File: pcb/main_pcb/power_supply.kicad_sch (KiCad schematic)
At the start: 36 parts, among them J12 Screw_Terminal_01x02, J13 Conn_01x02_Male, Q1 Q_PMOS_GDS, SW1 SW_SPDT, U1 LM3151/2/3, U5 TPIC74101

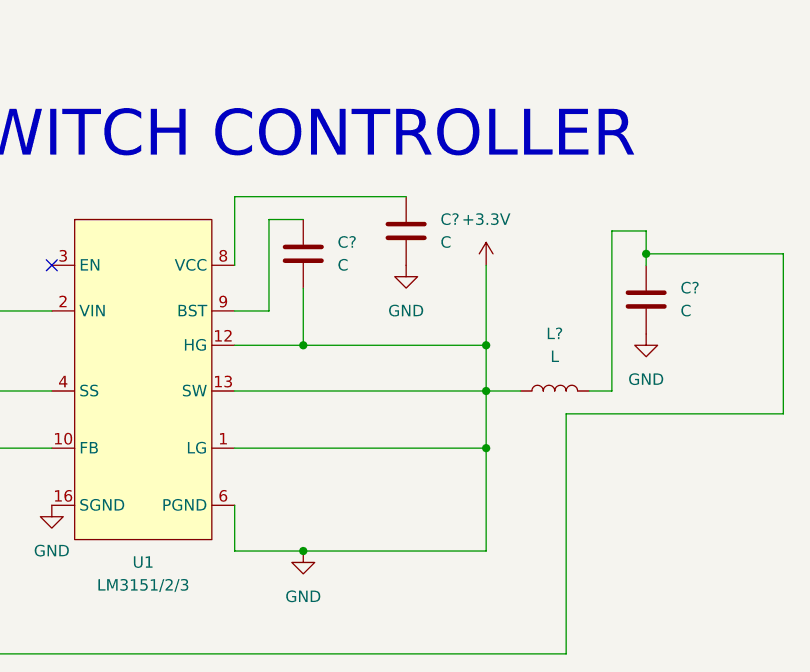
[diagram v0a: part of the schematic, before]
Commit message: ADDED MOSFETS
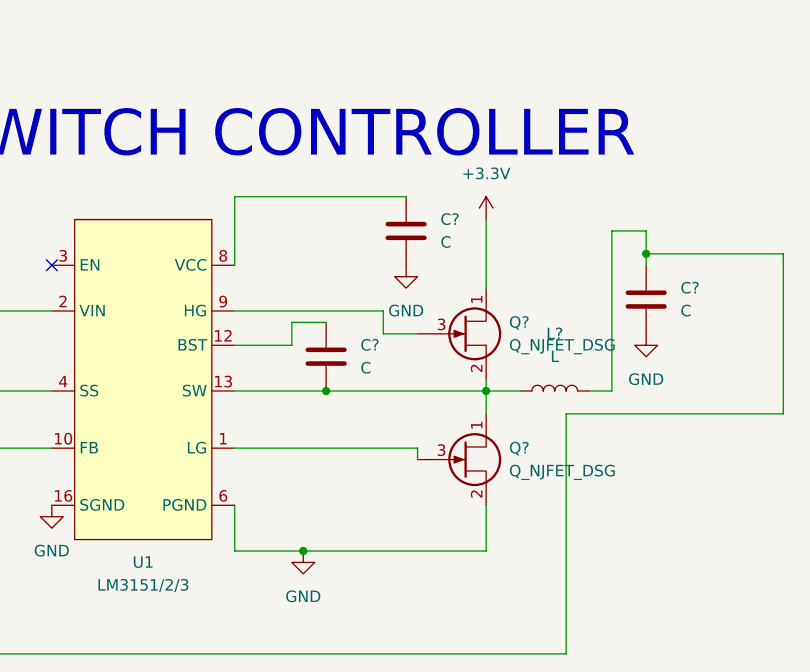
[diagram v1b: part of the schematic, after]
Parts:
- added Q? (x2): Q_NJFET_DSG, symbol Device:Q_NJFET_DSG
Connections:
- net +3.3V: now also Q?.1 (D); no longer C1.2, C10.2, C11.2, C13.2, C14.2, C15.2, C2.2, C3.2, C6.2, C7.2, C?.2, C?.2, C?.2, C?.2, C?.2, D4.2 (A), J12.1 (Pin_1), L?.2, Q1.1 (G), R10.1, R13.2, R7.1, R9.2, U1.1 (LG), U1.12 (HG), U1.13 (SW), U1.16 (SGND), U1.6 (PGND), U5.1 (SCR1), U5.11 (CLP), U5.16 (GND), U5.20 (SCR0), U5.21 (PAD), U5.6 (PGND)
- net at U1.9 (HG): now also Q?.3 (G); no longer C?.1
- new net: C?.2, L?.2, Q?.1 (D), Q?.2 (S), U1.13 (SW)
- new net: Q?.3 (G), U1.1 (LG)
- new net: C?.1, U1.12 (BST)
- new net GND: C1.2, C10.2, C11.2, C13.2, C14.2, C15.2, C2.2, C3.2, C6.2, C7.2, C?.2, C?.2, C?.2, C?.2, D4.2 (A), J12.1 (Pin_1), Q1.1 (G), Q?.2 (S), R10.1, R13.2, R7.1, R9.2, U1.16 (SGND), U1.6 (PGND), U5.1 (SCR1), U5.11 (CLP), U5.16 (GND), U5.20 (SCR0), U5.21 (PAD), U5.6 (PGND)
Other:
- moved on the sheet: C?
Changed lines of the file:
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@@
   (junction (at 139.7 43.815) (diameter 0) (color 0 0 0 0)
   )
-  (junction (at 142.24 156.21) (diameter 0) (color 0 0 0 0)
-  )
   (junction (at 142.24 179.07) (diameter 0) (color 0 0 0 0)
   )
@@
   (junction (at 213.36 71.12) (diameter 0) (color 0 0 0 0)
   )
+  (junction (at 144.78 161.29) (diameter 0) (color 0 0 0 0)
+  )
   (junction (at 137.16 87.63) (diameter 0) (color 0 0 0 0)
   )
@@
   )
   (junction (at 197.485 90.17) (diameter 0) (color 0 0 0 0)
-  )
-  (junction (at 162.56 156.21) (diameter 0) (color 0 0 0 0)
-  )
-  (junction (at 162.56 167.64) (diameter 0) (color 0 0 0 0)
   )
   (junction (at 225.425 51.435) (diameter 0) (color 0 0 0 0)
@@
     (stroke (width 0) (type default) (color 0 0 0 0))
   )
+  (wire (pts (xy 162.56 142.24) (xy 162.56 149.86))
+    (stroke (width 0) (type default) (color 0 0 0 0))
+  )
   (wire (pts (xy 70.485 50.165) (xy 70.485 43.815))
     (stroke (width 0) (type default) (color 0 0 0 0))
@@
     (stroke (width 0) (type default) (color 0 0 0 0))
   )
+  (wire (pts (xy 162.56 161.29) (xy 162.56 163.83))
+    (stroke (width 0) (type default) (color 0 0 0 0))
+  )
   (wire (pts (xy 161.925 91.44) (xy 161.925 98.425))
     (stroke (width 0) (type default) (color 0 0 0 0))
@@
     (stroke (width 0) (type default) (color 0 0 0 0))
   )
+  (wire (pts (xy 140.97 156.21) (xy 140.97 153.67))
+    (stroke (width 0) (type default) (color 0 0 0 0))
+  )
   (wire (pts (xy 179.07 46.355) (xy 180.975 46.355))
     (stroke (width 0) (type default) (color 0 0 0 0))
   )
+  (wire (pts (xy 134.62 167.64) (xy 154.94 167.64))
+    (stroke (width 0) (type default) (color 0 0 0 0))
+  )
   (wire (pts (xy 195.58 146.05) (xy 180.34 146.05))
     (stroke (width 0) (type default) (color 0 0 0 0))
@@
     (stroke (width 0) (type default) (color 0 0 0 0))
   )
-  (wire (pts (xy 142.24 149.86) (xy 142.24 156.21))
-    (stroke (width 0) (type default) (color 0 0 0 0))
-  )
   (wire (pts (xy 123.19 88.9) (xy 123.19 87.63))
     (stroke (width 0) (type default) (color 0 0 0 0))
@@
     (stroke (width 0) (type default) (color 0 0 0 0))
   )
-  (wire (pts (xy 162.56 147.32) (xy 162.56 156.21))
-    (stroke (width 0) (type default) (color 0 0 0 0))
-  )
   (wire (pts (xy 110.49 69.85) (xy 110.49 71.755))
     (stroke (width 0) (type default) (color 0 0 0 0))
@@
   )
   (wire (pts (xy 213.36 71.12) (xy 213.36 72.39))
+    (stroke (width 0) (type default) (color 0 0 0 0))
+  )
+  (wire (pts (xy 144.78 161.29) (xy 162.56 161.29))
     (stroke (width 0) (type default) (color 0 0 0 0))
   )
@@
     (stroke (width 0) (type default) (color 0 0 0 0))
   )
-  (wire (pts (xy 162.56 156.21) (xy 162.56 161.29))
+  (wire (pts (xy 151.13 154.94) (xy 154.94 154.94))
     (stroke (width 0) (type default) (color 0 0 0 0))
   )
@@
     (stroke (width 0) (type default) (color 0 0 0 0))
   )
-  (wire (pts (xy 162.56 167.64) (xy 162.56 179.07))
+  (wire (pts (xy 162.56 160.02) (xy 162.56 161.29))
+    (stroke (width 0) (type default) (color 0 0 0 0))
+  )
+  (wire (pts (xy 151.13 152.4) (xy 151.13 154.94))
     (stroke (width 0) (type default) (color 0 0 0 0))
   )
@@
   )
   (wire (pts (xy 123.19 80.01) (xy 172.085 80.01))
+    (stroke (width 0) (type default) (color 0 0 0 0))
+  )
+  (wire (pts (xy 162.56 173.99) (xy 162.56 179.07))
     (stroke (width 0) (type default) (color 0 0 0 0))
   )
@@
     (stroke (width 0) (type default) (color 0 0 0 0))
   )
-  (wire (pts (xy 134.62 156.21) (xy 142.24 156.21))
-    (stroke (width 0) (type default) (color 0 0 0 0))
-  )
   (wire (pts (xy 207.01 76.835) (xy 207.01 78.74))
     (stroke (width 0) (type default) (color 0 0 0 0))
@@
     (stroke (width 0) (type default) (color 0 0 0 0))
   )
-  (wire (pts (xy 134.62 161.29) (xy 162.56 161.29))
+  (wire (pts (xy 134.62 161.29) (xy 144.78 161.29))
     (stroke (width 0) (type default) (color 0 0 0 0))
   )
@@
     (stroke (width 0) (type default) (color 0 0 0 0))
   )
-  (wire (pts (xy 138.43 152.4) (xy 138.43 142.24))
-    (stroke (width 0) (type default) (color 0 0 0 0))
-  )
   (wire (pts (xy 190.5 48.895) (xy 190.5 46.355))
     (stroke (width 0) (type default) (color 0 0 0 0))
@@
     (stroke (width 0) (type default) (color 0 0 0 0))
   )
+  (wire (pts (xy 154.94 167.64) (xy 154.94 168.91))
+    (stroke (width 0) (type default) (color 0 0 0 0))
+  )
   (wire (pts (xy 154.305 96.52) (xy 154.305 98.425))
     (stroke (width 0) (type default) (color 0 0 0 0))
@@
     (stroke (width 0) (type default) (color 0 0 0 0))
   )
-  (wire (pts (xy 134.62 167.64) (xy 162.56 167.64))
-    (stroke (width 0) (type default) (color 0 0 0 0))
-  )
   (wire (pts (xy 67.31 57.785) (xy 67.31 59.69))
     (stroke (width 0) (type default) (color 0 0 0 0))
   )
-  (wire (pts (xy 134.62 152.4) (xy 138.43 152.4))
+  (wire (pts (xy 134.62 152.4) (xy 151.13 152.4))
     (stroke (width 0) (type default) (color 0 0 0 0))
   )
@@
     (stroke (width 0) (type default) (color 0 0 0 0))
   )
+  (wire (pts (xy 134.62 156.21) (xy 140.97 156.21))
+    (stroke (width 0) (type default) (color 0 0 0 0))
+  )
   (wire (pts (xy 197.485 43.815) (xy 197.485 40.005))
     (stroke (width 0) (type default) (color 0 0 0 0))
@@
     (stroke (width 0) (type default) (color 0 0 0 0))
   )
-  (wire (pts (xy 142.24 156.21) (xy 162.56 156.21))
-    (stroke (width 0) (type default) (color 0 0 0 0))
-  )
   (wire (pts (xy 238.125 81.28) (xy 225.425 81.28))
     (stroke (width 0) (type default) (color 0 0 0 0))
   )
-  (wire (pts (xy 138.43 142.24) (xy 142.24 142.24))
+  (wire (pts (xy 140.97 153.67) (xy 144.78 153.67))
     (stroke (width 0) (type default) (color 0 0 0 0))
   )
@@
   )
   (wire (pts (xy 190.5 43.815) (xy 190.5 46.355))
-    (stroke (width 0) (type default) (color 0 0 0 0))
-  )
-  (wire (pts (xy 162.56 161.29) (xy 162.56 167.64))
     (stroke (width 0) (type default) (color 0 0 0 0))
   )
@@
     )
     (property "Datasheet" "~" (id 3) (at 80.01 46.355 0)
+      (effects (font (size 1.27 1.27)) hide)
+    )
+    (pin "1")
+    (pin "2")
+    (pin "3")
+  )
+  (symbol (lib_id "Device:Q_NJFET_DSG") (at 160.02 154.94 0) (unit 1)
+    (in_bom yes) (on_board yes) (fields_autoplaced)
+    (property "Reference" "Q?" (id 0) (at 165.1 153.6699 0)
+      (effects (font (size 1.27 1.27)) (justify left))
+    )
+    (property "Value" "Q_NJFET_DSG" (id 1) (at 165.1 156.2099 0)
+      (effects (font (size 1.27 1.27)) (justify left))
+    )
+    (property "Footprint" "" (id 2) (at 165.1 152.4 0)
+      (effects (font (size 1.27 1.27)) hide)
+    )
+    (property "Datasheet" "~" (id 3) (at 160.02 154.94 0)
       (effects (font (size 1.27 1.27)) hide)
     )
@@
     (pin "1")
   )
+  (symbol (lib_id "Device:Q_NJFET_DSG") (at 160.02 168.91 0) (unit 1)
+    (in_bom yes) (on_board yes) (fields_autoplaced)
+    (property "Reference" "Q?" (id 0) (at 165.1 167.6399 0)
+      (effects (font (size 1.27 1.27)) (justify left))
+    )
+    (property "Value" "Q_NJFET_DSG" (id 1) (at 165.1 170.1799 0)
+      (effects (font (size 1.27 1.27)) (justify left))
+    )
+    (property "Footprint" "" (id 2) (at 165.1 166.37 0)
+      (effects (font (size 1.27 1.27)) hide)
+    )
+    (property "Datasheet" "~" (id 3) (at 160.02 168.91 0)
+      (effects (font (size 1.27 1.27)) hide)
+    )
+    (pin "1")
+    (pin "2")
+    (pin "3")
+  )
   (symbol (lib_id "Device:C") (at 123.19 57.15 0) (unit 1)
     (in_bom yes) (on_board yes) (fields_autoplaced)
@@
     (pin "1")
   )
-  (symbol (lib_id "power:+3.3V") (at 162.56 147.32 0) (unit 1)
-    (in_bom yes) (on_board yes) (fields_autoplaced)
-    (property "Reference" "#PWR?" (id 0) (at 162.56 151.13 0)
-      (effects (font (size 1.27 1.27)) hide)
-    )
-    (property "Value" "+3.3V" (id 1) (at 162.56 142.24 0))
-    (property "Footprint" "" (id 2) (at 162.56 147.32 0)
-      (effects (font (size 1.27 1.27)) hide)
-    )
-    (property "Datasheet" "" (id 3) (at 162.56 147.32 0)
-      (effects (font (size 1.27 1.27)) hide)
-    )
-    (pin "1")
-  )
-  (symbol (lib_id "Device:C") (at 142.24 146.05 0) (unit 1)
-    (in_bom yes) (on_board yes) (fields_autoplaced)
-    (property "Reference" "C?" (id 0) (at 146.05 144.7799 0)
-      (effects (font (size 1.27 1.27)) (justify left))
-    )
-    (property "Value" "C" (id 1) (at 146.05 147.3199 0)
-      (effects (font (size 1.27 1.27)) (justify left))
-    )
-    (property "Footprint" "" (id 2) (at 143.2052 149.86 0)
-      (effects (font (size 1.27 1.27)) hide)
-    )
-    (property "Datasheet" "~" (id 3) (at 142.24 146.05 0)
-      (effects (font (size 1.27 1.27)) hide)
-    )
+  (symbol (lib_id "power:+3.3V") (at 162.56 142.24 0) (unit 1)
+    (in_bom yes) (on_board yes) (fields_autoplaced)
+    (property "Reference" "#PWR?" (id 0) (at 162.56 146.05 0)
+      (effects (font (size 1.27 1.27)) hide)
+    )
+    (property "Value" "+3.3V" (id 1) (at 162.56 137.16 0))
+    (property "Footprint" "" (id 2) (at 162.56 142.24 0)
+      (effects (font (size 1.27 1.27)) hide)
+    )
+    (property "Datasheet" "" (id 3) (at 162.56 142.24 0)
+      (effects (font (size 1.27 1.27)) hide)
+    )
+    (pin "1")
+  )
+  (symbol (lib_id "Device:C") (at 144.78 157.48 0) (unit 1)
+    (in_bom yes) (on_board yes) (fields_autoplaced)
+    (property "Reference" "C?" (id 0) (at 148.59 156.2099 0)
+      (effects (font (size 1.27 1.27)) (justify left))
+    )
+    (property "Value" "C" (id 1) (at 148.59 158.7499 0)
+      (effects (font (size 1.27 1.27)) (justify left))
+    )
+    (property "Footprint" "" (id 2) (at 145.7452 161.29 0)
+      (effects (font (size 1.27 1.27)) hide)
+    )
+    (property "Datasheet" "~" (id 3) (at 144.78 157.48 0)
+      (effects (font (size 1.27 1.27)) hide)
+    )

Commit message: changes to pcb
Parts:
- removed C1: 330uF, Capacitor_SMD:CP_Elec_10x10.5, symbol Device:C_Polarized_US
- removed C10, C11, C2: 0.1uF, Capacitor_SMD:C_0603_1608Metric_Pad1.08x0.95mm_HandSolder, symbol Device:C
- removed C13: 100uF, Capacitor_SMD:CP_Elec_8x10.5, symbol Device:C_Polarized_US
- removed C14, C15: 22uF, Capacitor_SMD:CP_Elec_8x10.5, symbol Device:C_Polarized_US
- removed C3, C6: 470nF, Capacitor_SMD:C_0603_1608Metric_Pad1.08x0.95mm_HandSolder, symbol Device:C
- removed C7: 150nF, Capacitor_SMD:C_0603_1608Metric_Pad1.08x0.95mm_HandSolder, symbol Device:C
- removed C8, C9: 4.7nF, Capacitor_SMD:C_0603_1608Metric_Pad1.08x0.95mm_HandSolder, symbol Device:C
- removed D1, D2: LED, LED_THT:LED_D5.0mm, symbol Device:LED
- removed D4: D_Schottky, Diode_SMD:D_TUMD2, symbol Device:D_Schottky
- removed J12: Screw_Terminal_01x02, TerminalBlock:TerminalBlock_bornier-2_P5.08mm, symbol Connector:Screw_Terminal_01x02
- removed J13: Conn_01x02_Male, Connector_PinHeader_2.54mm:PinHeader_1x02_P2.54mm_Vertical, symbol Connector:Conn_01x02_Male
- removed L1, L2: 22uH, custom_footprints:L_SRR1050HA_Bourns, symbol Device:L
- removed Q1: Q_PMOS_GDS, Package_TO_SOT_SMD:TO-263-3_TabPin2, symbol Device:Q_PMOS_GDS
- removed R10: 0, Resistor_SMD:R_0603_1608Metric_Pad0.98x0.95mm_HandSolder, symbol Device:R
- removed R11, R12: 5k, Resistor_SMD:R_0603_1608Metric_Pad0.98x0.95mm_HandSolder, symbol Device:R
- removed R13: 470, Resistor_SMD:R_0603_1608Metric_Pad0.98x0.95mm_HandSolder, symbol Device:R
- removed R7: 12k, Resistor_SMD:R_0603_1608Metric_Pad0.98x0.95mm_HandSolder, symbol Device:R
- removed R8: 3.3k, Resistor_SMD:R_0603_1608Metric_Pad0.98x0.95mm_HandSolder, symbol Device:R
- removed R9: 4.53k, Resistor_SMD:R_0603_1608Metric_Pad0.98x0.95mm_HandSolder, symbol Device:R
- removed SW1: SW_SPDT, custom_footprints:SW_SPDT_NKK_MS12AANW03, symbol Switch:SW_SPDT
- removed U5: TPIC74101, custom_footprints:HTSSOP-20-1EP_4.4x6.5mm_P0.65mm_EP3.4x6.5mm_ThermalVias, symbol sym_library:TPIC74101
- gave numbers to parts that had none: 8
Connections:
- net +3.3V: no longer C1.1, U1.2 (VIN)
- net +BATT: now also C1.1, U1.2 (VIN)
- no-connect marks 2 -> 1
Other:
- note removed: "2.3V (min) * (3.3k + 4.53k) / 3.3k ~= 4V min"
- note removed: "BATTERY CONNECTION"
- note removed: "Battery input filtering"
- note removed: "Connect jumper for normal operation. Disconnect when Teensy is connected to USB"
- note removed: "DIGITAL 5V POWER SUPPLY"
- note removed: "Divider sets undervoltage"
- note removed: "Low-ESR"
- note removed: "MASTER POWER"
- note removed: "MOSFET for reverse input protection"
- note removed: "Max. 0.4V @ 1A @ 125ºC"
- note removed: "Minimize loop area"
- note removed: "OPTIONAL: LEDs Can use Red and Green LEDs to indicate battery polarity"
- note removed: "Sets switching freq."
- moved on the sheet: C1, C2, C3, C4, C5, L1, Q1, Q2, U1

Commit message: last minute changes
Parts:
- C1: value C -> 100 µF
- C2: value C -> 0.068 µF
- C3: value C -> 0.47 µF
- C4: value C -> 1 µF
- C5: value C -> 150 µF
- L1: value L -> 1.65 µH
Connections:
- net +3.3V is gone; now on net +BATT: Q1.1 (D)
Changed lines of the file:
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@@
       (effects (font (size 1.27 1.27)) (justify left))
     )
-    (property "Value" "C" (id 1) (at 163.83 64.7699 0)
+    (property "Value" "1 µF" (id 1) (at 163.83 64.7699 0)
       (effects (font (size 1.27 1.27)) (justify left))
     )
@@
     (in_bom yes) (on_board yes) (fields_autoplaced)
     (property "Reference" "L1" (id 0) (at 176.53 74.93 90))
-    (property "Value" "L" (id 1) (at 176.53 77.47 90))
+    (property "Value" "1.65 µH" (id 1) (at 176.53 77.47 90))
     (property "Footprint" "" (id 2) (at 176.53 81.28 0)
       (effects (font (size 1.27 1.27)) hide)
@@
       (effects (font (size 1.27 1.27)) (justify left))
     )
-    (property "Value" "C" (id 1) (at 190.5 72.3899 0)
+    (property "Value" "150 µF" (id 1) (at 190.5 72.3899 0)
       (effects (font (size 1.27 1.27)) (justify left))
     )
@@
     (pin "1")
   )
+  (symbol (lib_id "power:+BATT") (at 168.91 62.23 0) (unit 1)
+    (in_bom yes) (on_board yes) (fields_autoplaced)
+    (property "Reference" "#PWR?" (id 0) (at 168.91 66.04 0)
+      (effects (font (size 1.27 1.27)) hide)
+    )
+    (property "Value" "+BATT" (id 1) (at 171.45 60.9599 0)
+      (effects (font (size 1.27 1.27)) (justify left))
+    )
+    (property "Footprint" "" (id 2) (at 168.91 62.23 0)
+      (effects (font (size 1.27 1.27)) hide)
+    )
+    (property "Datasheet" "" (id 3) (at 168.91 62.23 0)
+      (effects (font (size 1.27 1.27)) hide)
+    )
+    (pin "1")
+  )
   (symbol (lib_id "Device:C") (at 101.6 85.09 0) (unit 1)
     (in_bom yes) (on_board yes) (fields_autoplaced)
@@
       (effects (font (size 1.27 1.27)) (justify left))
     )
-    (property "Value" "C" (id 1) (at 105.41 86.3599 0)
+    (property "Value" "0.068 µF" (id 1) (at 105.41 86.3599 0)
       (effects (font (size 1.27 1.27)) (justify left))
     )
@@
     (pin "1")
   )
-  (symbol (lib_id "power:+3.3V") (at 168.91 62.23 0) (unit 1)
-    (in_bom yes) (on_board yes) (fields_autoplaced)
-    (property "Reference" "#PWR0105" (id 0) (at 168.91 66.04 0)
-      (effects (font (size 1.27 1.27)) hide)
-    )
-    (property "Value" "+3.3V" (id 1) (at 168.91 57.15 0))
-    (property "Footprint" "" (id 2) (at 168.91 62.23 0)
-      (effects (font (size 1.27 1.27)) hide)
-    )
-    (property "Datasheet" "" (id 3) (at 168.91 62.23 0)
-      (effects (font (size 1.27 1.27)) hide)
-    )
-    (pin "1")
-  )
   (symbol (lib_id "Device:C") (at 151.13 77.47 0) (unit 1)
     (in_bom yes) (on_board yes) (fields_autoplaced)
@@
       (effects (font (size 1.27 1.27)) (justify left))
     )
-    (property "Value" "C" (id 1) (at 154.94 78.7399 0)
+    (property "Value" "0.47 µF" (id 1) (at 154.94 78.7399 0)
       (effects (font (size 1.27 1.27)) (justify left))
     )
@@
       (effects (font (size 1.27 1.27)) (justify left))
     )
-    (property "Value" "C" (id 1) (at 95.25 80.0099 0)
+    (property "Value" "100 µF" (id 1) (at 95.25 80.0099 0)
       (effects (font (size 1.27 1.27)) (justify left))
     )
